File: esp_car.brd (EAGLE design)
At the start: 81.6 x 84 mm, 52 parts, among them IC2 LT1963ES8-3.3, SW1 SK-12D01

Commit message: PDF,ガーバー出力
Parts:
- moved C2 1.02 mm to (10.5, 52.5)
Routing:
- net I2C_SDA: track 172.7 -> 140.2 mm, vias 3 -> 2
- net I2C_SCL: track 171.7 -> 145.7 mm, vias 2 -> 3
- net IO0: track 91.6 -> 83.1 mm, vias 4 -> 6
- net MR_IN2: track 15.8 -> 19.2 mm
- net N$6: track 67.6 -> 70.0 mm
- net MR_IN1: track 10.4 -> 12.0 mm
- net ML_IN2: track 16.1 -> 17.4 mm

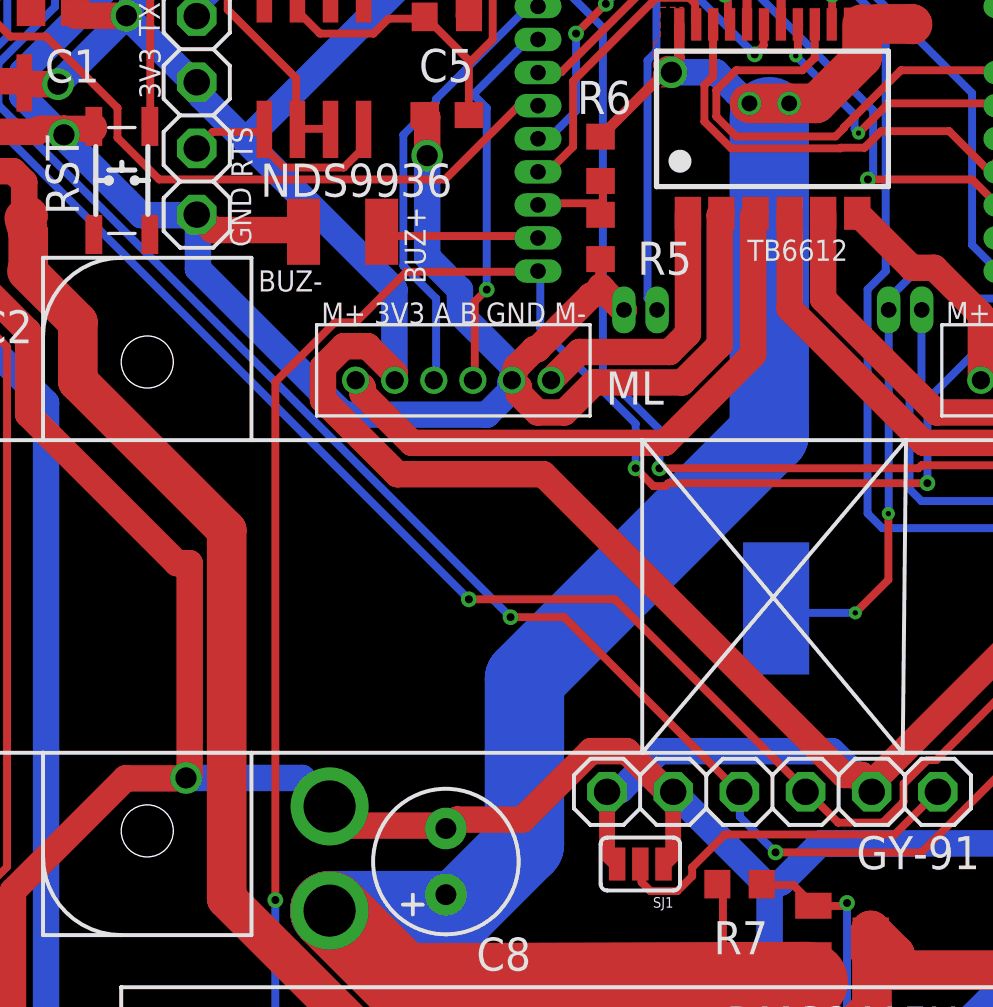
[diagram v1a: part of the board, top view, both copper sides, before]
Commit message: GNDを太く。サーマルランドが細かった
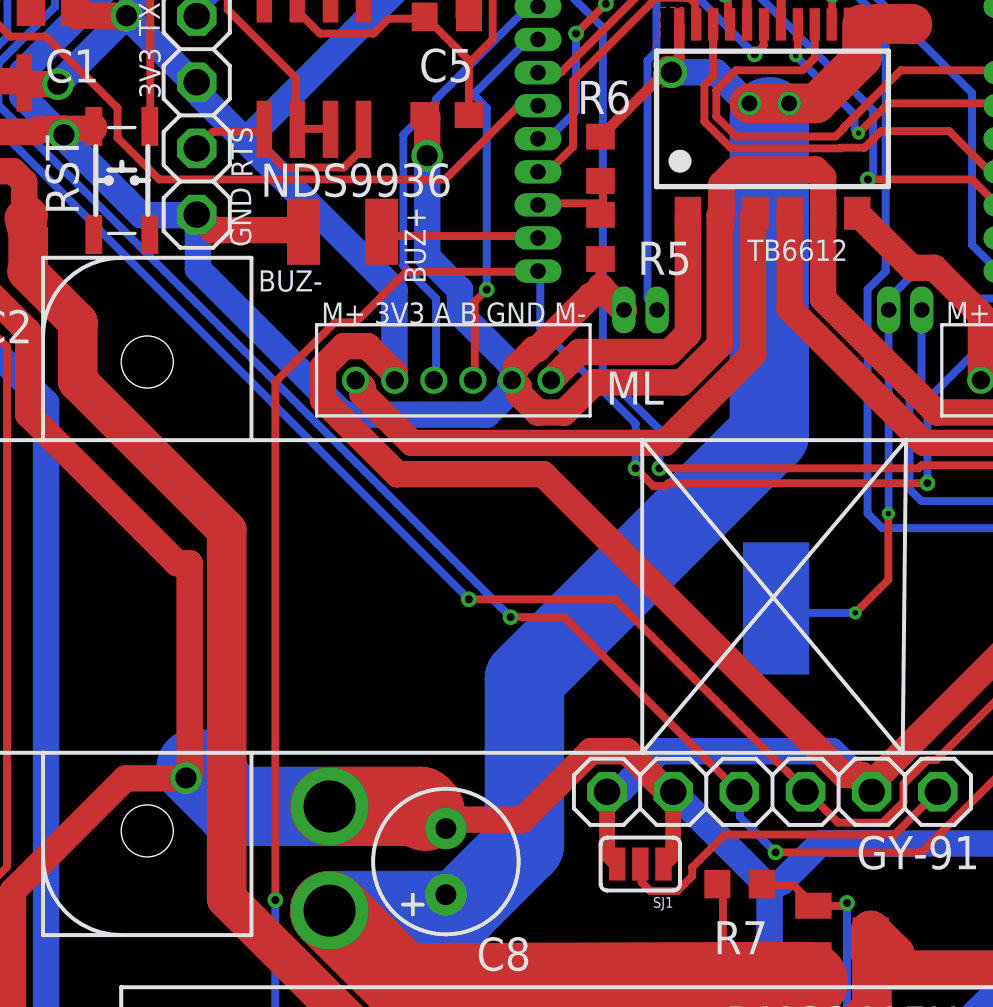
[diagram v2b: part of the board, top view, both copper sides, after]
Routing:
- net GND: track 443.0 -> 449.6 mm
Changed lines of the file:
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@@
 <wire x1="55.6641" y1="70.866" x2="54.7497" y2="69.9516" width="1.016" layer="16"/>
 <wire x1="55.6641" y1="72.6948" x2="55.6641" y2="70.866" width="1.016" layer="16"/>
-<wire x1="23.7744" y1="31.2039" x2="27.432" y2="31.2039" width="1.016" layer="1"/>
-<wire x1="23.0886" y1="31.8897" x2="23.7744" y2="31.2039" width="1.016" layer="1"/>
 <wire x1="27.432" y1="31.2039" x2="27.464" y2="31.093" width="1.016" layer="1"/>
-<wire x1="23.0886" y1="31.8897" x2="23" y2="31.94" width="1.016" layer="1"/>
 <wire x1="72.1233" y1="19.431" x2="72.4662" y2="19.431" width="1.016" layer="1"/>
 <wire x1="67.437" y1="14.7447" x2="69.1515" y2="16.4592" width="1.016" layer="1"/>
@@
 <wire x1="66.294" y1="25.2603" x2="70.1802" y2="29.1465" width="1.016" layer="1"/>
 <wire x1="72.3519" y1="54.5211" x2="72.39" y2="54.61" width="1.016" layer="1"/>
-<wire x1="21.9456" y1="33.0327" x2="17.4879" y2="33.0327" width="1.016" layer="16"/>
-<wire x1="22.9743" y1="32.004" x2="21.9456" y2="33.0327" width="1.016" layer="16"/>
-<wire x1="22.9743" y1="32.004" x2="23" y2="31.94" width="1.016" layer="16"/>
 <via x="12.8016" y="57.7215" extent="1-16" drill="0.8128"/>
 <via x="44.8056" y="66.1797" extent="1-16" drill="0.8128"/>
@@
 <wire x1="9.525" y1="52.07" x2="11.43" y2="50.165" width="1.016" layer="1"/>
 <wire x1="11.43" y1="46.99" x2="11.43" y2="50.165" width="1.016" layer="1"/>
+<wire x1="23" y1="31.94" x2="26.48" y2="31.94" width="3.048" layer="1"/>
+<wire x1="26.48" y1="31.94" x2="26.67" y2="31.75" width="3.048" layer="1"/>
+<wire x1="23" y1="31.94" x2="19.3479" y2="31.94" width="3.048" layer="16"/>
+<wire x1="19.3479" y1="31.94" x2="17.87155" y2="33.41635" width="3.048" layer="16"/>
+<wire x1="26.67" y1="31.75" x2="27.327" y2="31.093" width="0.3048" layer="1"/>
+<wire x1="27.327" y1="31.093" x2="27.464" y2="31.093" width="0.3048" layer="1"/>
+<wire x1="38.0402" y1="54.708" x2="38.0402" y2="55.8202" width="1.016" layer="1"/>
+<wire x1="41.656" y1="56.388" x2="38.608" y2="56.388" width="1.016" layer="1"/>
+<wire x1="38.0402" y1="55.8202" x2="38.608" y2="56.388" width="1.016" layer="1"/>
+<wire x1="41.946" y1="54.708" x2="41.946" y2="56.098" width="1.016" layer="1"/>
+<wire x1="41.946" y1="56.098" x2="41.656" y2="56.388" width="1.016" layer="1"/>
 </signal>
 <signal name="VDD" class="1">

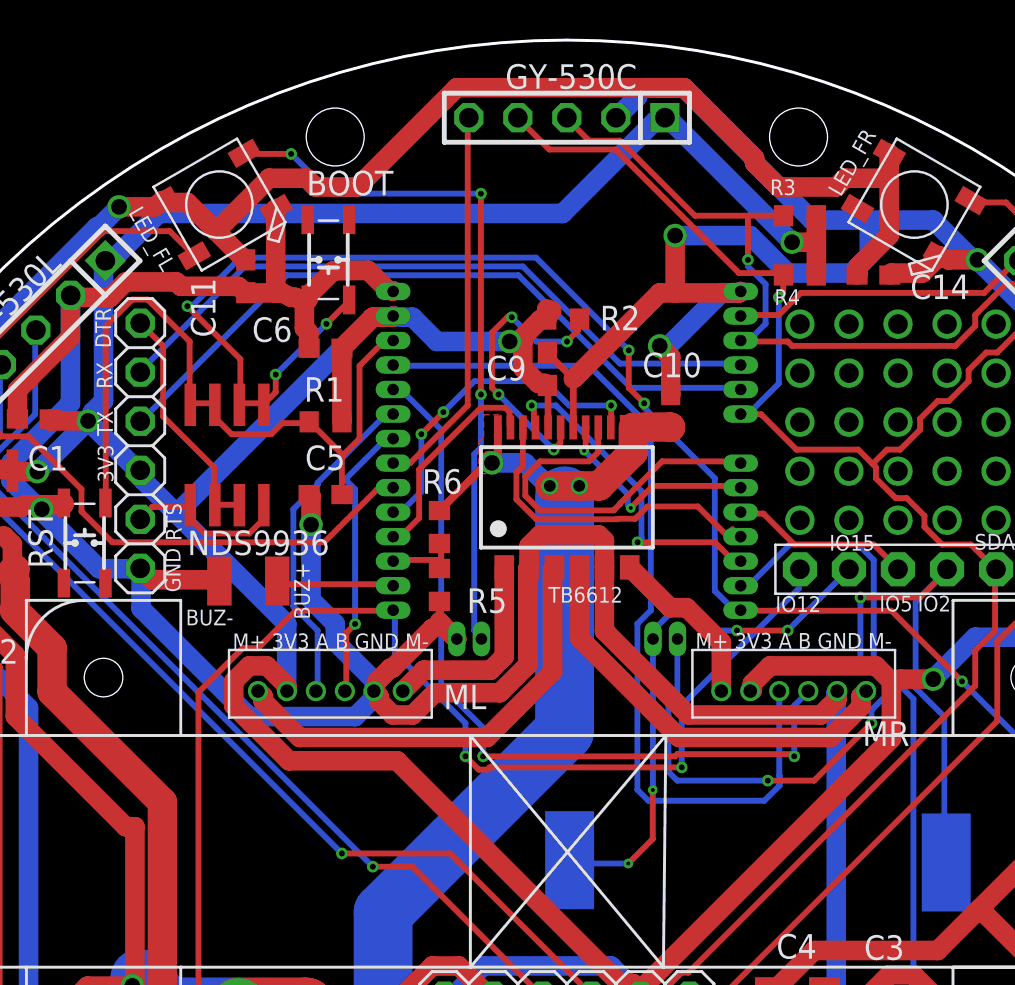
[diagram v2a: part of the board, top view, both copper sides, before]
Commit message: コンデンサの向きを修正
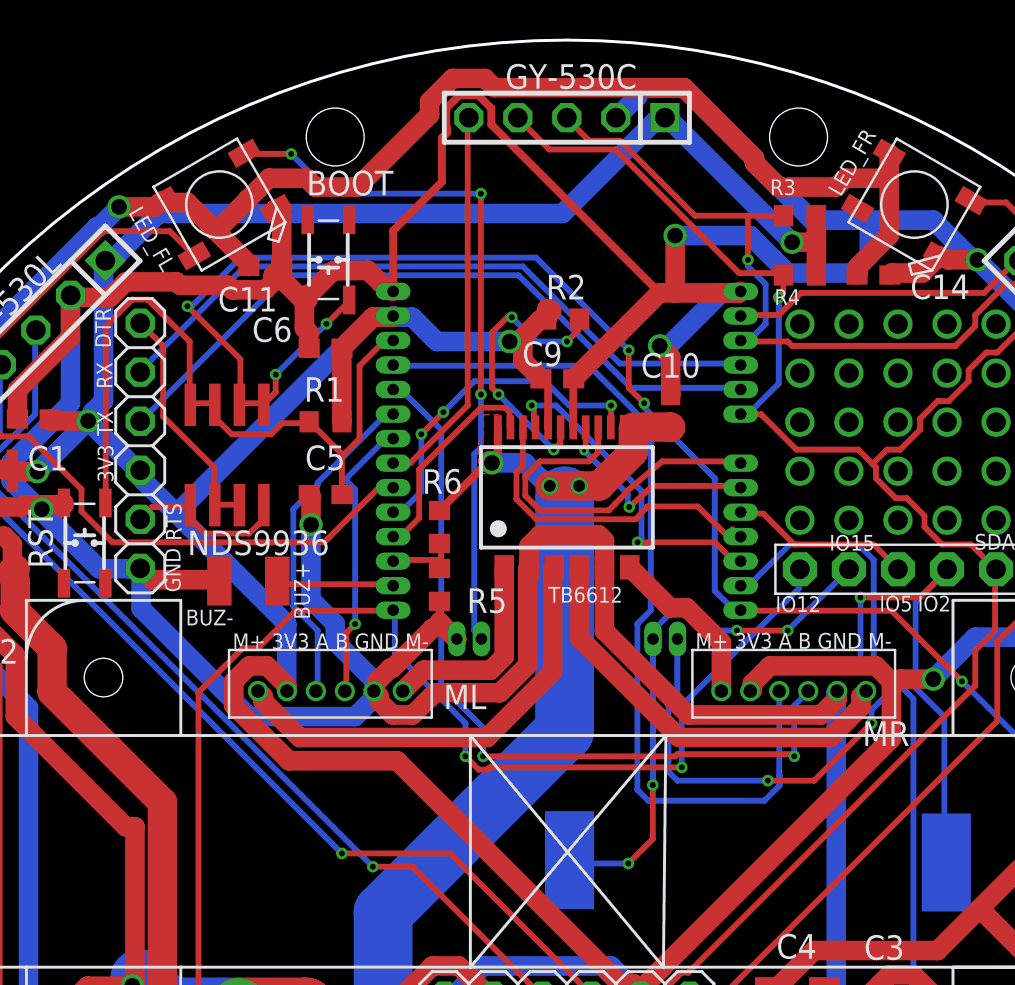
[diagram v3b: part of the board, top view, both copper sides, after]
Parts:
- moved C11 1.14 mm to (24.4, 70.3), turned to 0 degrees
- moved C9 0.72 mm to (39.5, 64.5), turned to 0 degrees
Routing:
- net GND: track 449.6 -> 474.8 mm
- net +5V: track 231.7 -> 232.9 mm

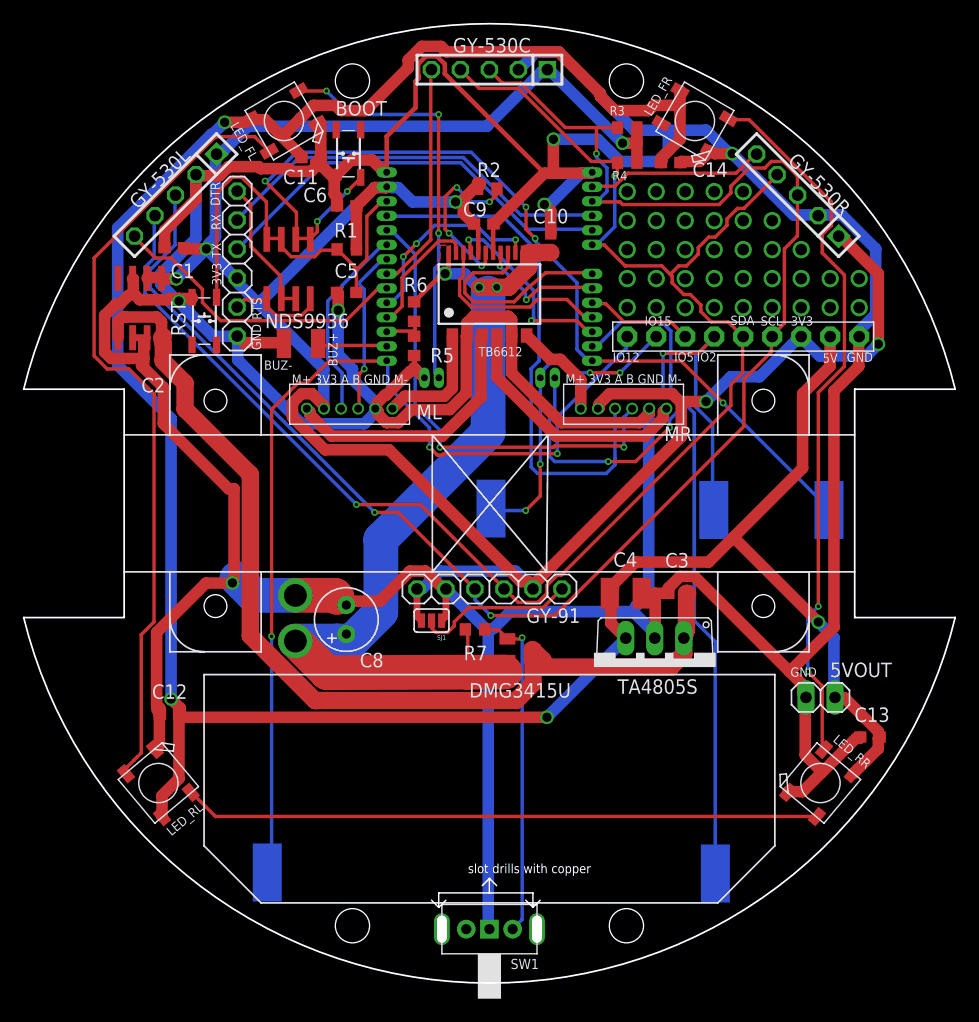
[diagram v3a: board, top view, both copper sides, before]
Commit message: c1,c9,r2,r3,r4 微修正　nmos向き修正、so8シルク追加
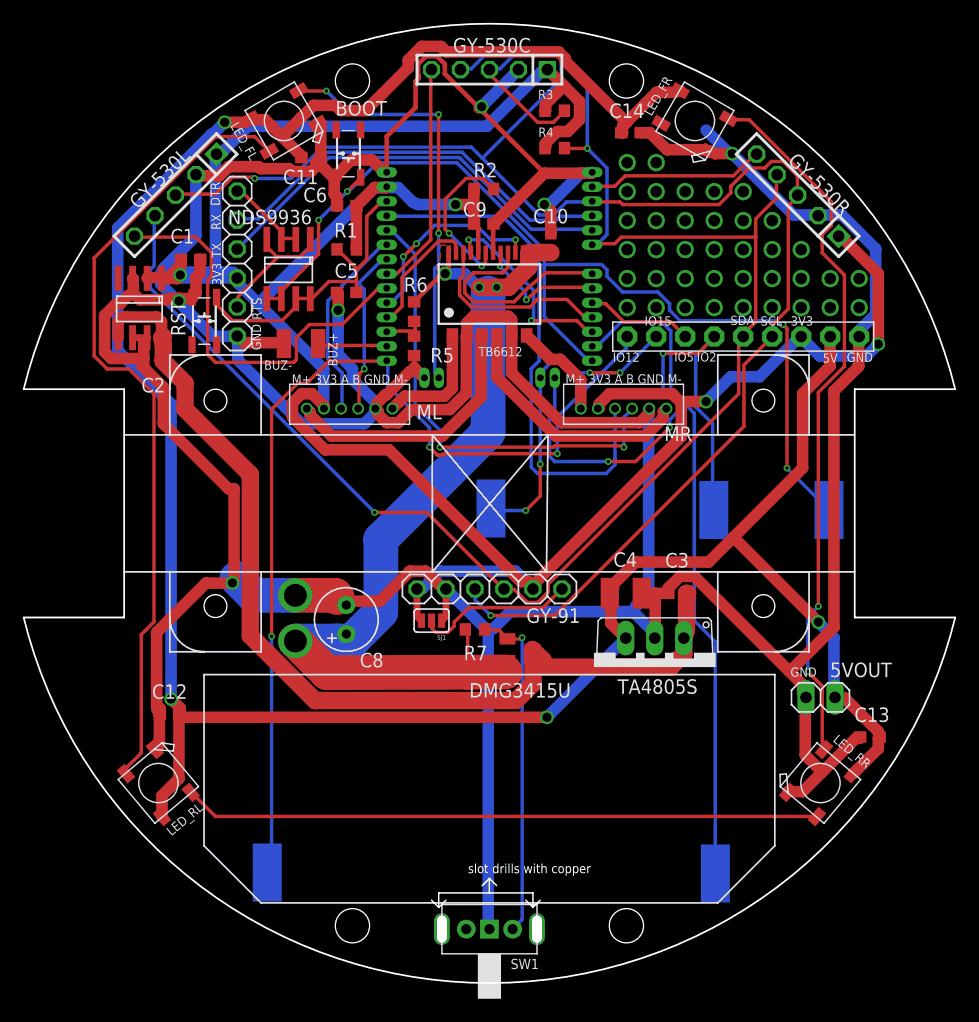
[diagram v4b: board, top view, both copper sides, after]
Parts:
- moved R3 6.52 mm to (45.7, 74.4), turned to 180 degrees
- moved R4 6.48 mm to (45.7, 71.1), turned to 180 degrees
- moved C14 4.35 mm to (52.4, 72.5)
- moved C1 1.76 mm to (13.8, 61.4), turned to 0 degrees
- moved R2 0.31 mm to (39.5, 67.5)
- turned NDS9936 to 180 degrees
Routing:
- net GND: track 474.8 -> 443.5 mm
- net EN: track 37.6 -> 27.1 mm
- net N$19: track 27.1 -> 36.3 mm
- net IO0: track 83.1 -> 89.6 mm, vias 6 -> 4
- net DTR: track 12.3 -> 7.42 mm
- net +5V: track 232.9 -> 228.4 mm
- net +3V3: track 227.2 -> 231.4 mm, vias 6 -> 4
- net I2C_SDA: track 140.2 -> 143.6 mm
- net RTS: track 8.76 -> 11.7 mm
- net N$7: track 14.9 -> 13.8 mm, vias 4 -> 2
- net TX: track 35.5 -> 36.2 mm
- net I2C_SCL: track 145.7 -> 145.2 mm, vias 3 -> 2
